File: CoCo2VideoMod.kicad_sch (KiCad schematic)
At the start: 39 parts, among them J1 20261043, J2 to PCB, J3 Video, J4 GND_S, J5 GND_W, J6 GND_N, Q1 BC547, Q2 BC557, Q3 BC547, Q4 BC557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

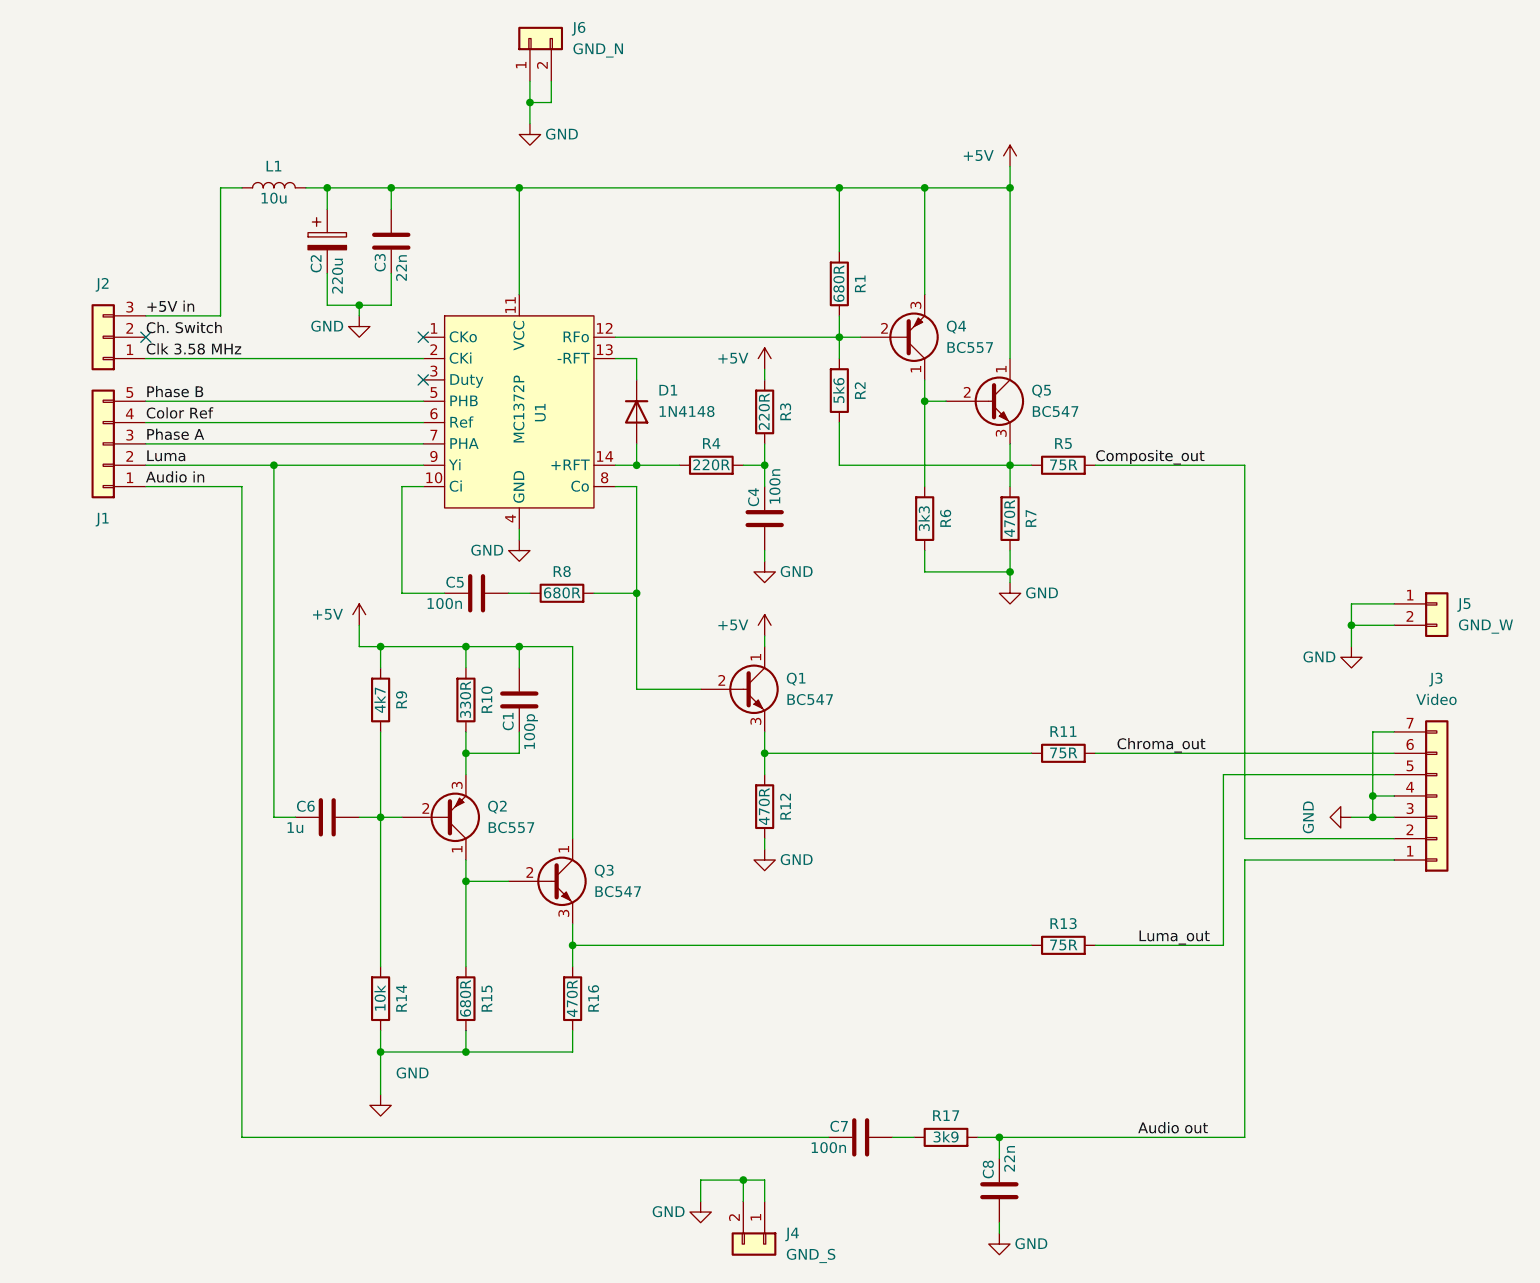
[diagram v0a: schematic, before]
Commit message: adjusted GND pin position, added PCB description to silk screen, started README
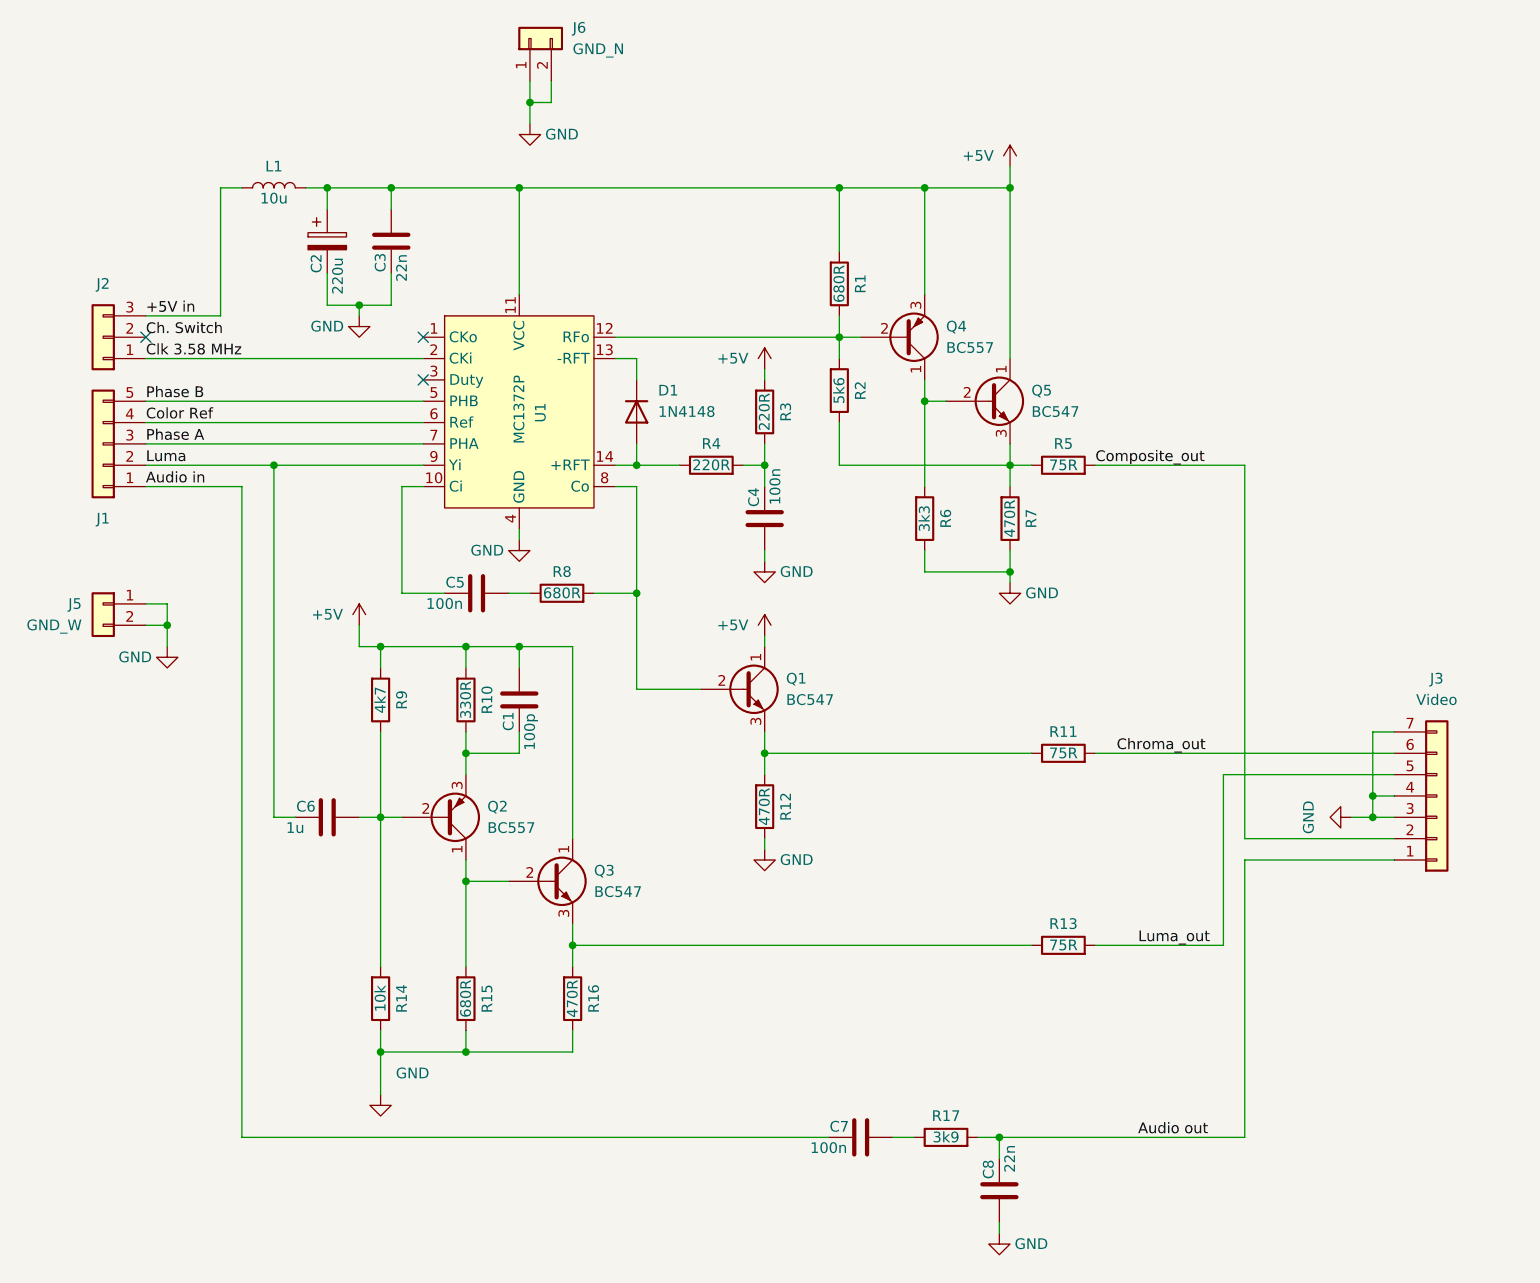
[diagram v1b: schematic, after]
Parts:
- removed J4: GND_S, Connector_PinHeader_2.54mm:PinHeader_1x02_P2.54mm_Vertical, symbol Connector_Generic:Conn_01x02
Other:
- moved on the sheet: J5
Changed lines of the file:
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@@
     (company "Riven Hexagon Electronics")
   )
-  (junction (at 185.42 90.17) (diameter 0) (color 0 0 0 0)
-  )
   (junction (at 80.01 140.97) (diameter 0) (color 0 0 0 0)
   )
@@
   (junction (at 69.85 140.97) (diameter 0) (color 0 0 0 0)
   )
+  (junction (at 44.45 90.17) (diameter 0) (color 0 0 0 0)
+  )
   (junction (at 143.51 151.13) (diameter 0) (color 0 0 0 0)
-  )
-  (junction (at 113.03 156.21) (diameter 0) (color 0 0 0 0)
   )
   (junction (at 86.36 38.1) (diameter 0) (color 0 0 0 0)
@@
     (stroke (width 0) (type default))
   )
+  (wire (pts (xy 41.91 90.17) (xy 44.45 90.17))
+    (stroke (width 0) (type default))
+  )
   (wire (pts (xy 92.71 128.27) (xy 147.32 128.27))
     (stroke (width 0) (type default))
@@
     (stroke (width 0) (type default))
   )
-  (wire (pts (xy 185.42 90.17) (xy 185.42 92.71))
-    (stroke (width 0) (type default))
-  )
   (wire (pts (xy 115.57 81.28) (xy 115.57 82.55))
     (stroke (width 0) (type default))
@@
     (stroke (width 0) (type default))
   )
-  (wire (pts (xy 107.95 156.21) (xy 113.03 156.21))
-    (stroke (width 0) (type default))
-  )
   (wire (pts (xy 69.85 113.03) (xy 69.85 102.87))
     (stroke (width 0) (type default))
@@
     (stroke (width 0) (type default))
   )
-  (wire (pts (xy 107.95 158.75) (xy 107.95 156.21))
-    (stroke (width 0) (type default))
-  )
   (wire (pts (xy 170.18 107.95) (xy 170.18 128.27))
     (stroke (width 0) (type default))
@@
     (stroke (width 0) (type default))
   )
-  (wire (pts (xy 185.42 87.63) (xy 190.5 87.63))
-    (stroke (width 0) (type default))
-  )
   (wire (pts (xy 60.96 38.1) (xy 63.5 38.1))
     (stroke (width 0) (type default))
@@
     (stroke (width 0) (type default))
   )
+  (wire (pts (xy 44.45 87.63) (xy 44.45 90.17))
+    (stroke (width 0) (type default))
+  )
   (wire (pts (xy 124.46 71.12) (xy 124.46 66.04))
     (stroke (width 0) (type default))
@@
     (stroke (width 0) (type default))
   )
-  (wire (pts (xy 185.42 90.17) (xy 185.42 87.63))
-    (stroke (width 0) (type default))
-  )
   (wire (pts (xy 53.34 73.66) (xy 53.34 151.13))
     (stroke (width 0) (type default))
@@
     (stroke (width 0) (type default))
   )
-  (wire (pts (xy 115.57 156.21) (xy 113.03 156.21))
-    (stroke (width 0) (type default))
-  )
   (wire (pts (xy 187.96 102.87) (xy 190.5 102.87))
     (stroke (width 0) (type default))
@@
     (stroke (width 0) (type default))
   )
-  (wire (pts (xy 190.5 90.17) (xy 185.42 90.17))
-    (stroke (width 0) (type default))
-  )
   (wire (pts (xy 67.31 92.71) (xy 67.31 90.17))
     (stroke (width 0) (type default))
@@
     (stroke (width 0) (type default))
   )
+  (wire (pts (xy 44.45 90.17) (xy 44.45 92.71))
+    (stroke (width 0) (type default))
+  )
   (wire (pts (xy 154.94 105.41) (xy 190.5 105.41))
     (stroke (width 0) (type default))
@@
     (stroke (width 0) (type default))
   )
+  (wire (pts (xy 41.91 87.63) (xy 44.45 87.63))
+    (stroke (width 0) (type default))
+  )
   (wire (pts (xy 57.15 71.12) (xy 74.93 71.12))
     (stroke (width 0) (type default))
@@
     (stroke (width 0) (type default))
   )
-  (wire (pts (xy 113.03 156.21) (xy 113.03 158.75))
-    (stroke (width 0) (type default))
-  )
   (wire (pts (xy 41.91 58.42) (xy 74.93 58.42))
     (stroke (width 0) (type default))
@@
   )
   (wire (pts (xy 187.96 110.49) (xy 187.96 113.03))
-    (stroke (width 0) (type default))
-  )
-  (wire (pts (xy 115.57 158.75) (xy 115.57 156.21))
     (stroke (width 0) (type default))
   )
@@
         (path "/e26cf8f1-b9bc-4bc2-a425-d53c73655768"
           (reference "#PWR07") (unit 1)
-        )
-      )
-    )
-  )
-  (symbol (lib_id "Connector_Generic:Conn_01x02") (at 115.57 163.83 270) (unit 1)
-    (in_bom yes) (on_board yes) (dnp no) (fields_autoplaced)
-    (property "Reference" "J4" (at 118.11 162.56 90)
-      (effects (font (size 1.27 1.27)) (justify left))
-    )
-    (property "Value" "GND_S" (at 118.11 165.1 90)
-      (effects (font (size 1.27 1.27)) (justify left))
-    )
-    (property "Footprint" "Connector_PinHeader_2.54mm:PinHeader_1x02_P2.54mm_Vertical" (at 115.57 163.83 0)
-      (effects (font (size 1.27 1.27)) hide)
-    )
-    (property "Datasheet" "~" (at 115.57 163.83 0)
-      (effects (font (size 1.27 1.27)) hide)
-    )
-    (pin "1")
-    (pin "2")
-    (instances
-      (project "CoCo2VideoMod"
-        (path "/e26cf8f1-b9bc-4bc2-a425-d53c73655768"
-          (reference "J4") (unit 1)
         )
       )
@@
     )
   )
-  (symbol (lib_id "power:GND") (at 107.95 158.75 0) (unit 1)
-    (in_bom yes) (on_board yes) (dnp no)
-    (property "Reference" "#PWR013" (at 107.95 165.1 0)
-      (effects (font (size 1.27 1.27)) hide)
-    )
-    (property "Value" "GND" (at 104.14 160.02 0)
-      (effects (font (size 1.27 1.27)))
-    )
-    (property "Footprint" "" (at 107.95 158.75 0)
-      (effects (font (size 1.27 1.27)) hide)
-    )
-    (property "Datasheet" "" (at 107.95 158.75 0)
-      (effects (font (size 1.27 1.27)) hide)
-    )
-    (pin "1")
-    (instances
-      (project "CoCo2VideoMod"
-        (path "/e26cf8f1-b9bc-4bc2-a425-d53c73655768"
-          (reference "#PWR013") (unit 1)
-        )
-      )
-    )
-  )
   (symbol (lib_id "Device:R") (at 151.13 128.27 90) (unit 1)
     (in_bom yes) (on_board yes) (dnp no)
@@
     )
   )
-  (symbol (lib_id "Connector_Generic:Conn_01x02") (at 195.58 87.63 0) (unit 1)
-    (in_bom yes) (on_board yes) (dnp no) (fields_autoplaced)
-    (property "Reference" "J5" (at 198.12 87.63 0)
+  (symbol (lib_id "Connector_Generic:Conn_01x02") (at 36.83 87.63 0) (mirror y) (unit 1)
+    (in_bom yes) (on_board yes) (dnp no)
+    (property "Reference" "J5" (at 34.29 87.63 0)
       (effects (font (size 1.27 1.27)) (justify left))
     )
-    (property "Value" "GND_W" (at 198.12 90.17 0)
+    (property "Value" "GND_W" (at 34.29 90.17 0)
       (effects (font (size 1.27 1.27)) (justify left))
     )
-    (property "Footprint" "Connector_PinHeader_2.54mm:PinHeader_1x02_P2.54mm_Vertical" (at 195.58 87.63 0)
-      (effects (font (size 1.27 1.27)) hide)
-    )
-    (property "Datasheet" "~" (at 195.58 87.63 0)
+    (property "Footprint" "Connector_PinHeader_2.54mm:PinHeader_1x02_P2.54mm_Vertical" (at 36.83 87.63 0)
+      (effects (font (size 1.27 1.27)) hide)
+    )
+    (property "Datasheet" "~" (at 36.83 87.63 0)
       (effects (font (size 1.27 1.27)) hide)
     )
@@
     )
   )
-  (symbol (lib_id "power:GND") (at 185.42 92.71 0) (unit 1)
-    (in_bom yes) (on_board yes) (dnp no)
-    (property "Reference" "#PWR014" (at 185.42 99.06 0)
-      (effects (font (size 1.27 1.27)) hide)
-    )
-    (property "Value" "GND" (at 181.61 93.98 0)
-      (effects (font (size 1.27 1.27)))
-    )
-    (property "Footprint" "" (at 185.42 92.71 0)
-      (effects (font (size 1.27 1.27)) hide)
-    )
-    (property "Datasheet" "" (at 185.42 92.71 0)
-      (effects (font (size 1.27 1.27)) hide)
-    )
+  (symbol (lib_id "power:GND") (at 44.45 92.71 0) (unit 1)
+    (in_bom yes) (on_board yes) (dnp no)
+    (property "Reference" "#PWR014" (at 44.45 99.06 0)
+      (effects (font (size 1.27 1.27)) hide)
+    )
+    (property "Value" "GND" (at 40.64 93.98 0)
+      (effects (font (size 1.27 1.27)))
+    )
+    (property "Footprint" "" (at 44.45 92.71 0)
+      (effects (font (size 1.27 1.27)) hide)
+    )
+    (property "Datasheet" "" (at 44.45 92.71 0)
+      (effects (font (size 1.27 1.27)) hide)
+    )
